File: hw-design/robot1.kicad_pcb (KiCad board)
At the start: 2 copper layers, 63.5 x 26.7 mm, 75 parts, among them P1 test-double, P2 CONN_01X04, P3 CONN_01X03, P4 left_motor, P5 right_motor, P6 CONN_01X05, P7 CONN_01X05, U1 STM32F072CB / STM32F042C6, U2 usb-micro, U3 MCP73833, U4 AP111733, U5 drv8835, U6 drv8835, U7 BlueNRG, U8 BALF-NRG-01D3, Y1 16MHz, Y2 32kHz, Y3 16MHz

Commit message: Routing complete?
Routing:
- net +3V3: track 123.8 -> 242.3 mm, vias 11 -> 23
- net /micro/led3: track 0.00 -> 45.3 mm, vias 0 -> 6
- net +BATT: track 33.8 -> 67.5 mm, vias 2 -> 4
- net GND: track 258.2 -> 281.5 mm, vias 50 -> 49
- net Net-(P1-Pad1): track 14.4 -> 16.9 mm
- net /micro/aphaser: track 6.44 -> 8.65 mm
- net /micro/progress: track 38.1 -> 37.0 mm
- net /bluetooth/ble_resetn: track 33.0 -> 34.0 mm
- net /bluetooth/ble_spi_cs: track 32.2 -> 33.1 mm
- net Net-(P7-Pad2): track 31.1 -> 32.0 mm
- net /bluetooth/ble_spi_clk: track 24.0 -> 24.7 mm
- net /micro/bphaser: track 8.29 -> 7.76 mm
- net Net-(P6-Pad4): track 37.8 -> 38.4 mm
- net /micro/led4: track 40.0 -> 40.5 mm

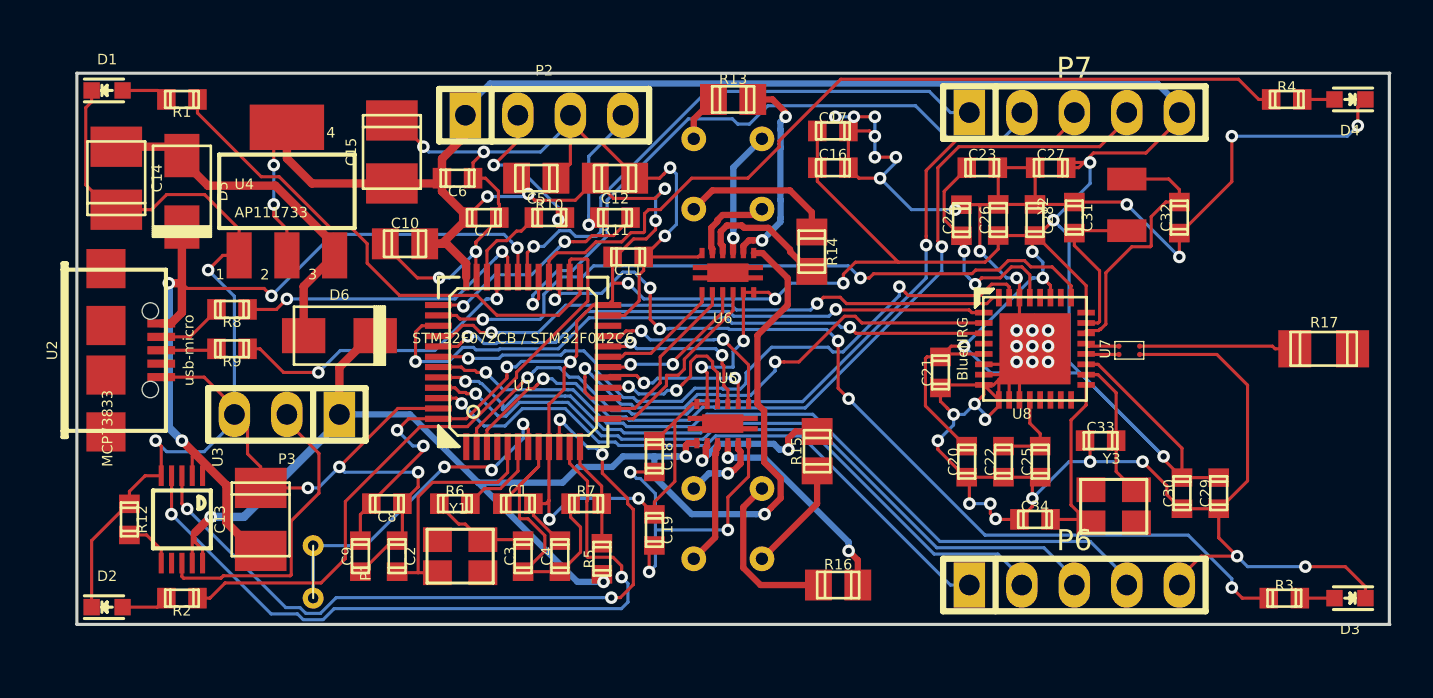
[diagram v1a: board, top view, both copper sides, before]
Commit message: Groud planes improved
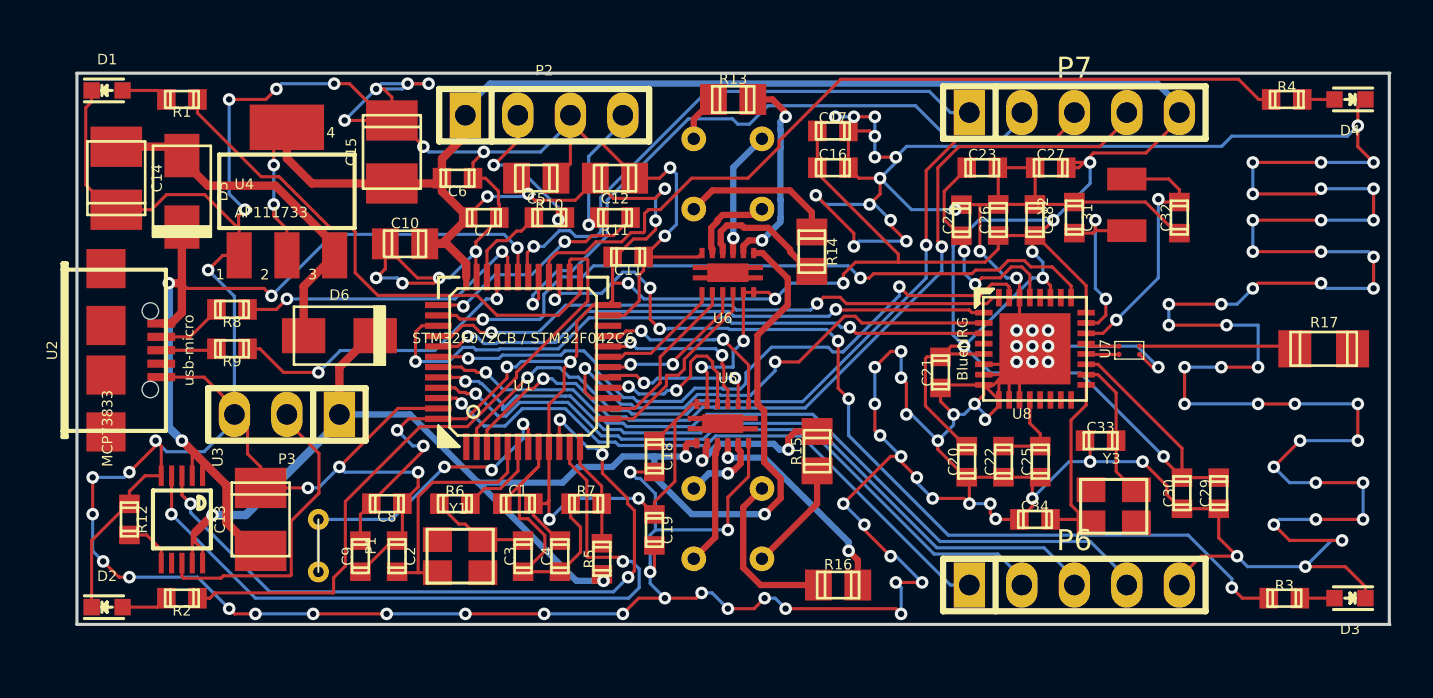
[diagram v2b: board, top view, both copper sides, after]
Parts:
- moved P1 1.30 mm to (152.7, 138.4)
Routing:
- net GND: track 281.5 -> 496.2 mm, vias 49 -> 129
- net +3V3: track 242.3 -> 239.1 mm
- net Net-(C31-Pad1): track 8.05 -> 9.64 mm, vias 0 -> 2
- net /micro/progress: track 37.0 -> 35.8 mm
- net /micro/led3: track 45.3 -> 46.4 mm
- net Net-(P1-Pad1): track 16.9 -> 16.1 mm
- net /micro/led2: track 30.3 -> 31.0 mm
- net /micro/led1: track 25.0 -> 25.6 mm
- net Net-(C32-Pad1): track 12.9 -> 12.8 mm, vias 0 -> 2

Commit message: Mounting holes for additional wheels or whatever
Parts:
- removed D6: D_Schottky, w_smd_diode:do214ac
- added P8: CONN_01X01, Mounting_Holes:MountingHole_2.2mm_M2_ISO7380, F.Cu at (195.6, 129.0)
- added P9: CONN_01X01, Mounting_Holes:MountingHole_2.2mm_M2_ISO7380, F.Cu at (149.8, 128.9)
- D5: footprint w_smd_diode:do214ac -> iwasz:sod123-pins21
- moved R8 6.74 mm to (155.2, 127.5)
- moved R9 6.73 mm to (155.2, 129.3)
- moved D5 0.63 mm to (146.1, 120.7), turned to 90 degrees
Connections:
- C14 pad 1: Net-(C14-Pad1) -> +BATT
- D5 pad 1: Net-(C14-Pad1) -> +BATT
- U4 pad 3: Net-(C14-Pad1) -> +BATT
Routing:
- net Net-(C14-Pad1): track 17.7 -> 0.00 mm
- net +BATT: track 67.5 -> 85.0 mm, vias 4 -> 6
- net GND: track 496.2 -> 506.5 mm
- net Net-(R9-Pad1): track 2.70 -> 11.3 mm
- net Net-(R8-Pad1): track 3.25 -> 10.6 mm
- net Net-(R8-Pad2): track 14.8 -> 8.31 mm
- net Net-(R9-Pad2): track 15.1 -> 9.87 mm
- net Net-(R17-Pad2): track 7.62 -> 9.52 mm
- net +5V: track 42.7 -> 44.4 mm

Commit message: patlabor logo
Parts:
- added P10: CONN_01X01, iwasz:patlabor1, F.Cu at (187.5, 129.0)
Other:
- board text added: "+BATT"
- board text added: "3V3"
- board text added: "CLK"
- board text added: "GND"
- board text added: "IO"
- board text added: "PA8"
- board text added: "PA9"
- board text added: "PB7"
- board text added: "PB8"
- board text added: "PB9"
- board text added: "PC13"
- board text added: "PC14"
- board text added: "PF11"
- board text added: "reset"
- board text added: "therm"

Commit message: Napisy, obrqazek
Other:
- board text added: "dla Frania"
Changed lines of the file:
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@@
-(kicad_pcb (version 4) (host pcbnew 0.201604271216+6712~44~ubuntu15.10.1-product)
+(kicad_pcb (version 4) (host pcbnew 4.1.0-alpha+201605041001+6771~44~ubuntu15.10.1-product)
   (general
     (links 194)
@@
     (area 140.894999 115.494999 204.575001 142.315001)
     (thickness 1.6)
-    (drawings 26)
+    (drawings 28)
     (tracks 1611)
     (zones 0)
@@
     (pad_to_mask_clearance 0.2)
     (aux_axis_origin 0 0)
-    (visible_elements FFFFEF7F)
+    (visible_elements FFFFFF7F)
     (pcbplotparams
       (layerselection 0x00030_ffffffff)
@@
     (at 187.325 122.67184 270)
     (descr "SMT capacitor, 0603")
-    (fp_text reference C28 (at 2.29616 0.381 360) (layer F.SilkS)
+    (fp_text reference C28 (at 2.29616 0.381) (layer F.SilkS)
       (effects (font (size 0.508 0.508) (thickness 0.0508)))
     )
@@
     (at 189.23 122.555 270)
     (descr "SMT capacitor, 0603")
-    (fp_text reference C31 (at 1.651 0 360) (layer F.SilkS)
+    (fp_text reference C31 (at 1.651 0) (layer F.SilkS)
       (effects (font (size 0.508 0.508) (thickness 0.0508)))
     )
@@
       (xy -0.912798 3.799906) (xy -0.831576 3.776739) (xy -0.566228 3.739397) (xy -0.330957 3.751622)) (layer F.SilkS) (width 0.01))
   )
+  (gr_text "dla Frania" (at 179.705 132.08 90) (layer F.SilkS)
+    (effects (font (size 1.5 1.5) (thickness 0.3)))
+  )
+  (dimension 22.86 (width 0.3) (layer Dwgs.User)
+    (gr_text "0,9000 in" (at 210.265 128.905 270) (layer Dwgs.User)
+      (effects (font (size 1.5 1.5) (thickness 0.3)))
+    )
+    (feature1 (pts (xy 194.31 140.335) (xy 211.615 140.335)))
+    (feature2 (pts (xy 194.31 117.475) (xy 211.615 117.475)))
+    (crossbar (pts (xy 208.915 117.475) (xy 208.915 140.335)))
+    (arrow1a (pts (xy 208.915 140.335) (xy 208.328579 139.208496)))
+    (arrow1b (pts (xy 208.915 140.335) (xy 209.501421 139.208496)))
+    (arrow2a (pts (xy 208.915 117.475) (xy 208.328579 118.601504)))
+    (arrow2b (pts (xy 208.915 117.475) (xy 209.501421 118.601504)))
+  )
   (gr_text 3V3 (at 194.31 119.38) (layer F.SilkS)

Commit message: Motors spin
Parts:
- removed P10: CONN_01X01, iwasz:patlabor1
- R6: value R -> 220R
- U1: value STM32F072CB / STM32F042C6 -> STM32F072CB/F042C6
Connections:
- U1 pad 20: /micro/aenblr -> Net-(U1-Pad20)
- U1 pad 21: /micro/benblr -> /micro/aenblr
- U1 pad 22: Net-(U1-Pad22) -> /micro/benblr
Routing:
- net GND: track 506.5 -> 513.6 mm
- net /micro/aenblr: track 8.34 -> 9.02 mm

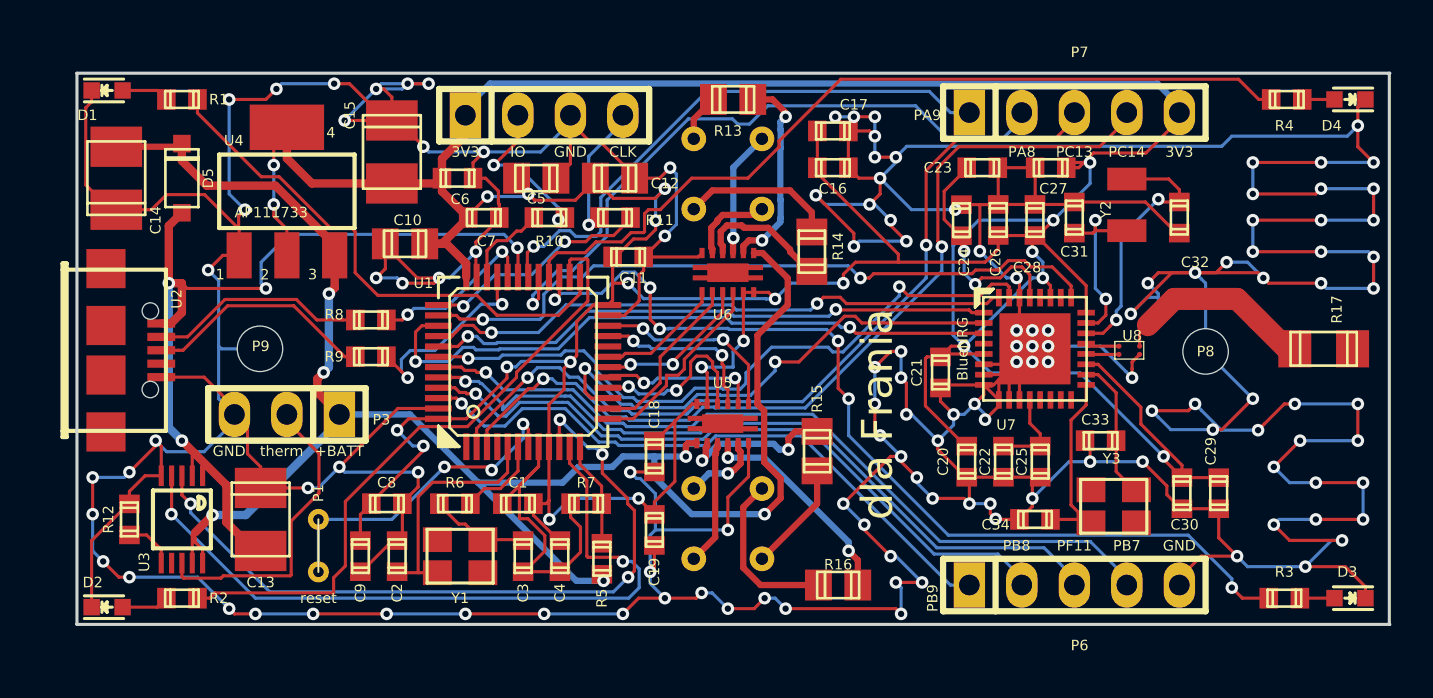
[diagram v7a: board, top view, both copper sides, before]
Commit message: Docs, PCB modified (problems with RF and low speed oscillator)
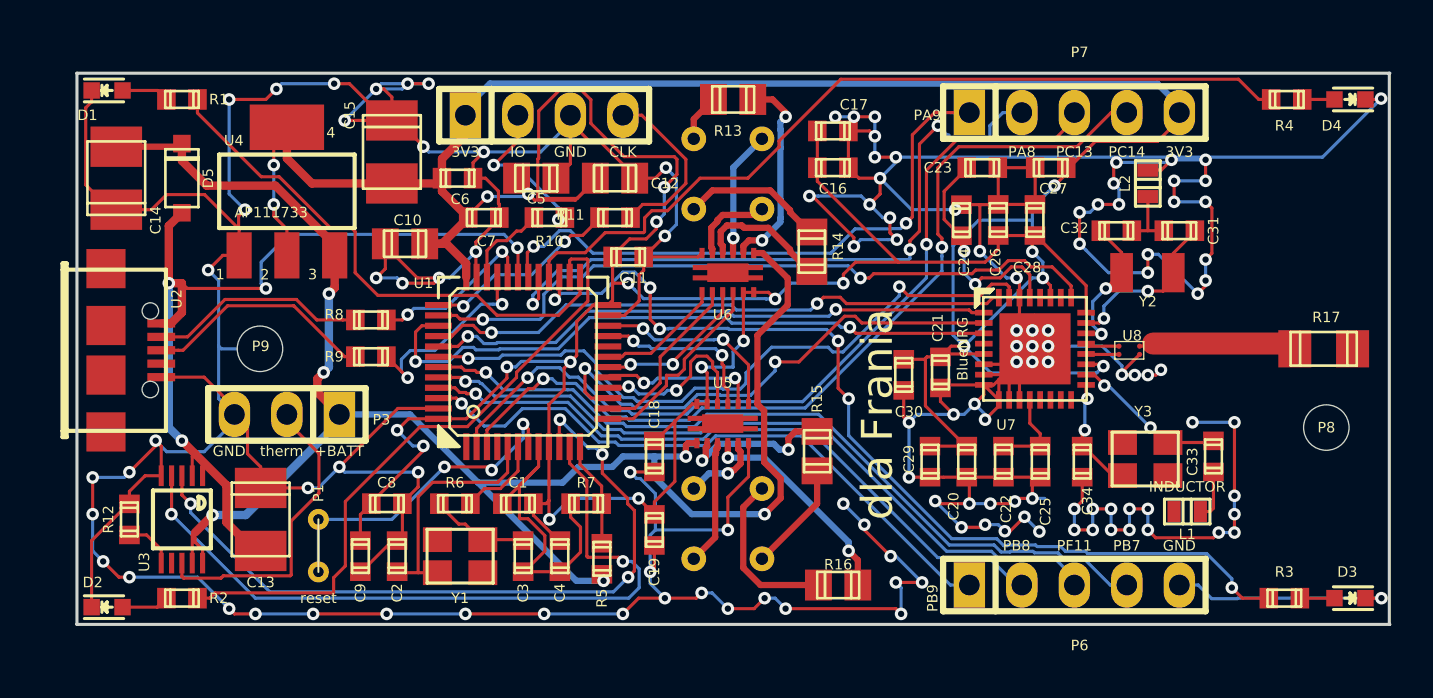
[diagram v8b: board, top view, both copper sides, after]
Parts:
- added L1: INDUCTOR, w_smd_inductors:inductor_smd_0603, F.Cu at (194.7, 136.8)
- added L2: 3.9 nH, w_smd_inductors:inductor_smd_0603, F.Cu at (192.8, 120.9)
- moved C30 14.6 mm to (181.0, 130.2)
- moved C29 14.1 mm to (182.2, 134.4)
- moved Y2 7.85 mm to (192.8, 128.5), turned to 0 degrees
- moved P8 6.91 mm to (201.4, 132.7)
- moved C33 5.51 mm to (196.0, 134.1), turned to 90 degrees
- moved C31 5.12 mm to (194.3, 123.2), turned to 0 degrees
- moved C34 3.61 mm to (189.6, 134.4), turned to 90 degrees
- moved C32 3.11 mm to (191.3, 123.2), turned to 180 degrees
- moved Y3 2.75 mm to (192.7, 134.2)
- turned R11 to 0 degrees
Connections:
- C31 pad 2: GND -> Net-(C31-Pad2)
- C32 pad 2: GND -> Net-(C31-Pad2)
- C33 pad 2: GND -> Net-(C33-Pad2)
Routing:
- net GND: track 513.6 -> 436.4 mm, vias 129 -> 125
- net Net-(C32-Pad1): track 12.8 -> 6.92 mm
- net Net-(C34-Pad1): track 9.46 -> 5.63 mm, vias 0 -> 2
- net Net-(C31-Pad2): track 0.00 -> 3.19 mm
- net Net-(C33-Pad2): track 0.00 -> 2.45 mm
- net Net-(P2-Pad4): track 6.66 -> 8.83 mm, vias 1 -> 0
- net Net-(R17-Pad2): track 9.94 -> 7.79 mm
- net Net-(P7-Pad1): track 27.4 -> 29.5 mm, vias 1 -> 2
- net /micro/swdclk: track 11.1 -> 9.63 mm
- net Net-(C31-Pad1): track 9.64 -> 8.27 mm
- net Net-(P7-Pad2): track 32.0 -> 33.2 mm, vias 1 -> 3
- net +3V3: track 239.1 -> 240.1 mm, vias 23 -> 22
- net Net-(P6-Pad2): track 33.3 -> 32.6 mm
- net Net-(P6-Pad3): track 36.2 -> 35.5 mm
- net Net-(C33-Pad1): track 6.98 -> 7.58 mm, vias 0 -> 2
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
